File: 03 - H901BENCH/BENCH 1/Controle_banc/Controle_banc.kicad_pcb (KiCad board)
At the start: 2 copper layers, 67 x 61.5 mm, 17 parts, among them J1 6P Droit 22-11-2062, J2 2P Droit 22-11-2022, J3 2P Droit 22-11-2022, J4 Connecteur Pcan 5747844-6, J5 4P Droit 22-11-2042

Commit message: modif legere carte
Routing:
- net /GND: track 151.2 -> 0.00 mm
- net /CANH: track 41.7 -> 54.6 mm

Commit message: Update carte controle banc + maj fs rules
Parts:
- removed R4: 680, EPSA_lib:RESC3216X70N
- added R5: 680, Resistor_THT:R_Axial_DIN0207_L6.3mm_D2.5mm_P10.16mm_Horizontal, F.Cu at (119.5, 31.0)
- R1, R2, R3: footprint EPSA_lib:RESC3216X70N -> Resistor_THT:R_Axial_DIN0207_L6.3mm_D2.5mm_P10.16mm_Horizontal
- moved R1 9.12 mm to (136.5, 41.1), turned to 90 degrees
- moved LED2 6.36 mm to (129.5, 47.9)
- moved LED3 6.34 mm to (117.0, 47.9)
- moved LED1 6.32 mm to (143.0, 46.1)
- moved S1 4.29 mm to (152.0, 44.5)
- moved R2 3.97 mm to (143.5, 30.9), turned to -90 degrees
- moved R3 3.12 mm to (129.5, 30.9)
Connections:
- net /GND renamed GND
- J1 pad 1: /12V -> +12V
- J2 pad 1: /12V -> +12V
- J5 pad 4: /12V -> +12V
- R2 pad 1: Net-(R2-Pad1) -> +12V
- R2 pad 2: /12V -> Net-(R2-Pad2)
- R3 pad 1: /12V -> +12V
- S1 pad 1: Net-(R2-Pad1) -> Net-(R2-Pad2)
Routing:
- net /GNDLog: track 45.6 -> 141.5 mm
- net /CANL: track 36.4 -> 119.1 mm
- net /12V: track 73.7 -> 0.00 mm
- net +12V: track 0.00 -> 67.6 mm
- net /CANH: track 54.6 -> 93.4 mm
- net /FRG/RUN: track 58.6 -> 34.0 mm
- net Net-(R2-Pad2): track 0.00 -> 9.03 mm
- net Net-(R2-Pad1): track 8.19 -> 0.00 mm
- net /RFE: track 20.4 -> 28.4 mm
- net /BTB: track 11.0 -> 8.21 mm
- net Net-(LED3-A): track 3.45 -> 6.19 mm
- net Net-(LED1-A): track 11.7 -> 10.7 mm
- net Net-(LED2-A): track 3.45 -> 4.27 mm
- added copper zone on B.Cu, net GND
- removed copper zone on F.Cu, net GND
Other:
- outline, holes or cut-outs redrawn

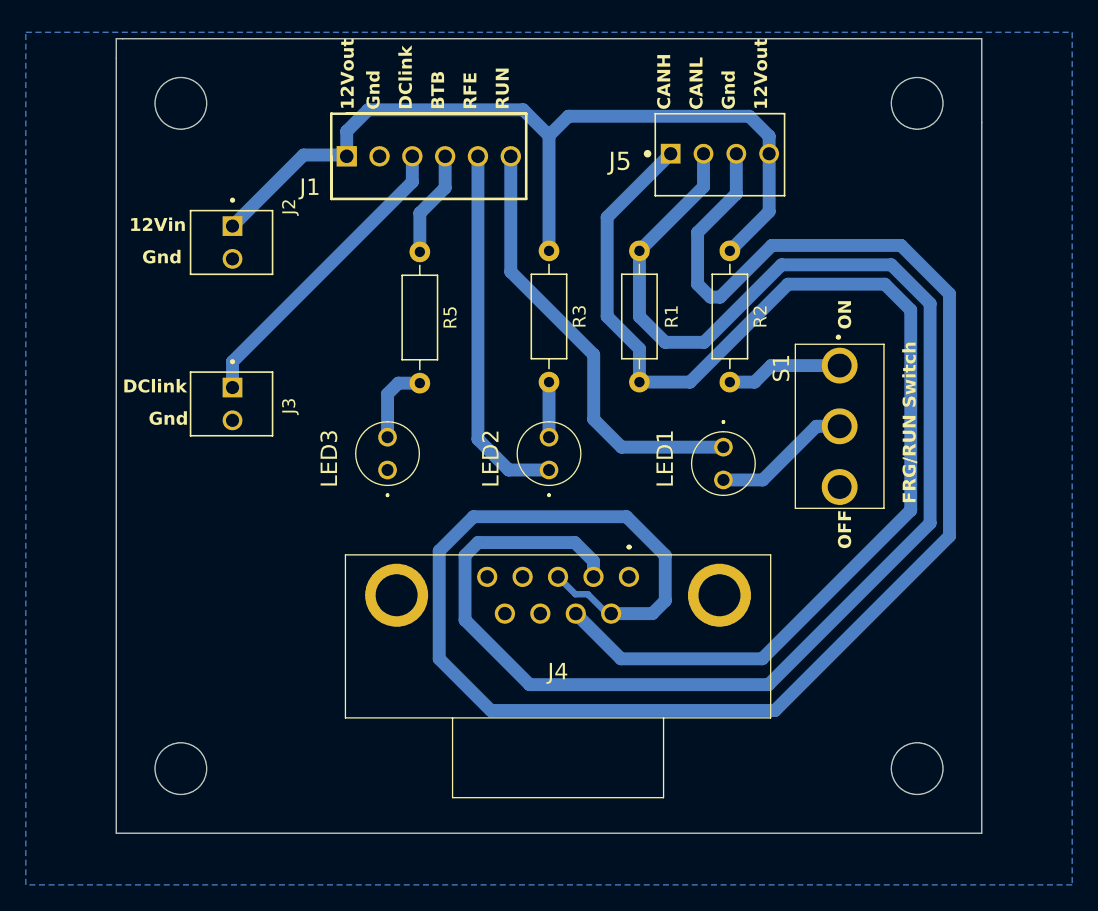
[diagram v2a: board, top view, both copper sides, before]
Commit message: Maj carte controle banc avec borniers
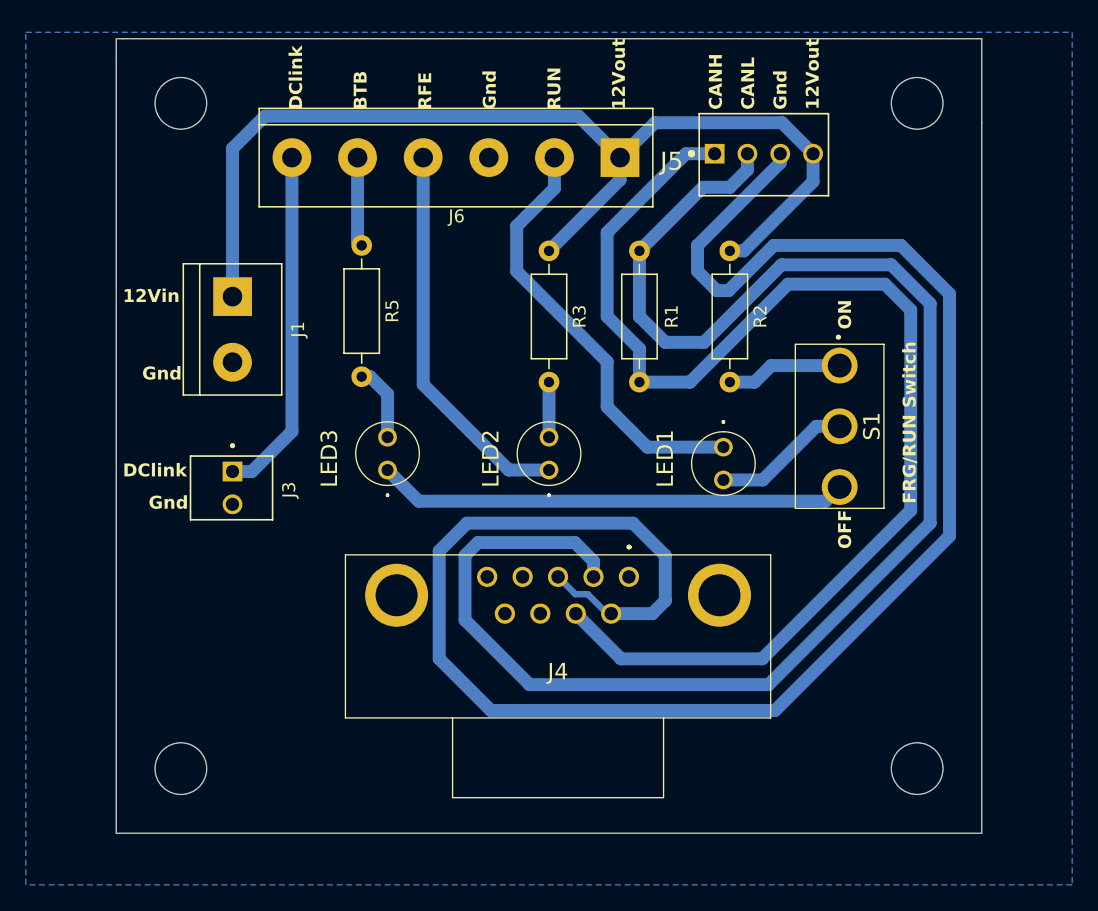
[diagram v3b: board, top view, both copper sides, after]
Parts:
- removed J2: 2P Droit 22-11-2022, EPSA_lib:MOLEX_22-11-2022
- added J6: Screw_Terminal_01x06, TerminalBlock:TerminalBlock_bornier-6_P5.08mm, F.Cu at (135.0, 23.7)
- J1: value 6P Droit 22-11-2062 -> Screw_Terminal_01x02; footprint EPSA_lib:HDRV6W87P0X254_1X6_1509X635X1092P -> TerminalBlock:TerminalBlock_bornier-2_P5.08mm
- J4: footprint EPSA_lib:57478446 -> EPSA:57478446
- LED1, LED2, LED3: footprint EPSA_lib:4302H55V -> EPSA:4302H55V
- S1: footprint EPSA_lib:100SP1T1B4M2QE -> EPSA:100SP1T1B4M2QE
- moved J1 14.0 mm to (105.0, 34.5), turned to -90 degrees
- moved J3 6.50 mm to (105.0, 48.0)
- moved R5 4.53 mm to (115.0, 30.5)
- moved J5 3.40 mm to (146.1, 23.4)
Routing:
- net GND: track 0.00 -> 36.5 mm
- net +12V: track 67.6 -> 81.2 mm
- net /DC-link: track 23.7 -> 27.1 mm
- net /CANH: track 93.4 -> 96.1 mm
- net /CANL: track 119.1 -> 121.8 mm
- net /RFE: track 28.4 -> 30.0 mm
- net /BTB: track 8.21 -> 7.07 mm
